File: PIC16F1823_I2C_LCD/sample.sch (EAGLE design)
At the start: 16 parts, among them CN1 12V_IN, CN2 PIC_CN_H, SW1 10-XX, U1 XC6202P502TB, U2 PIC16F1823-I/P, U3 AE-AQM1602A

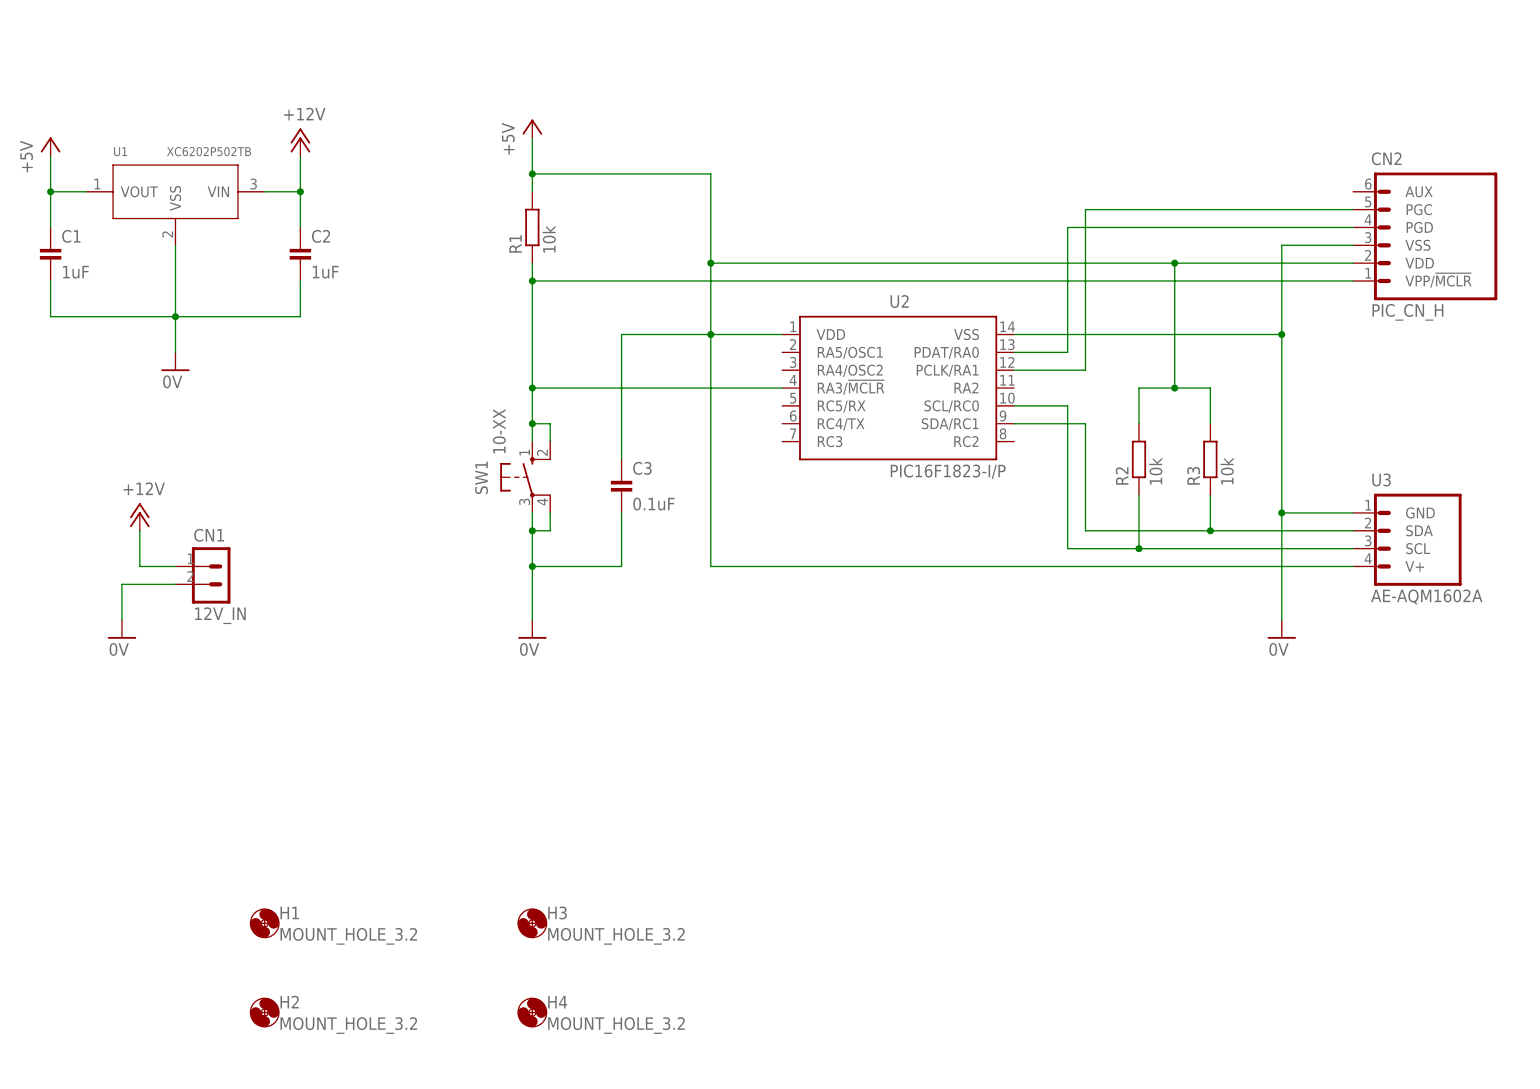
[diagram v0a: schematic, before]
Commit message: 回路図を3.3Vに修正
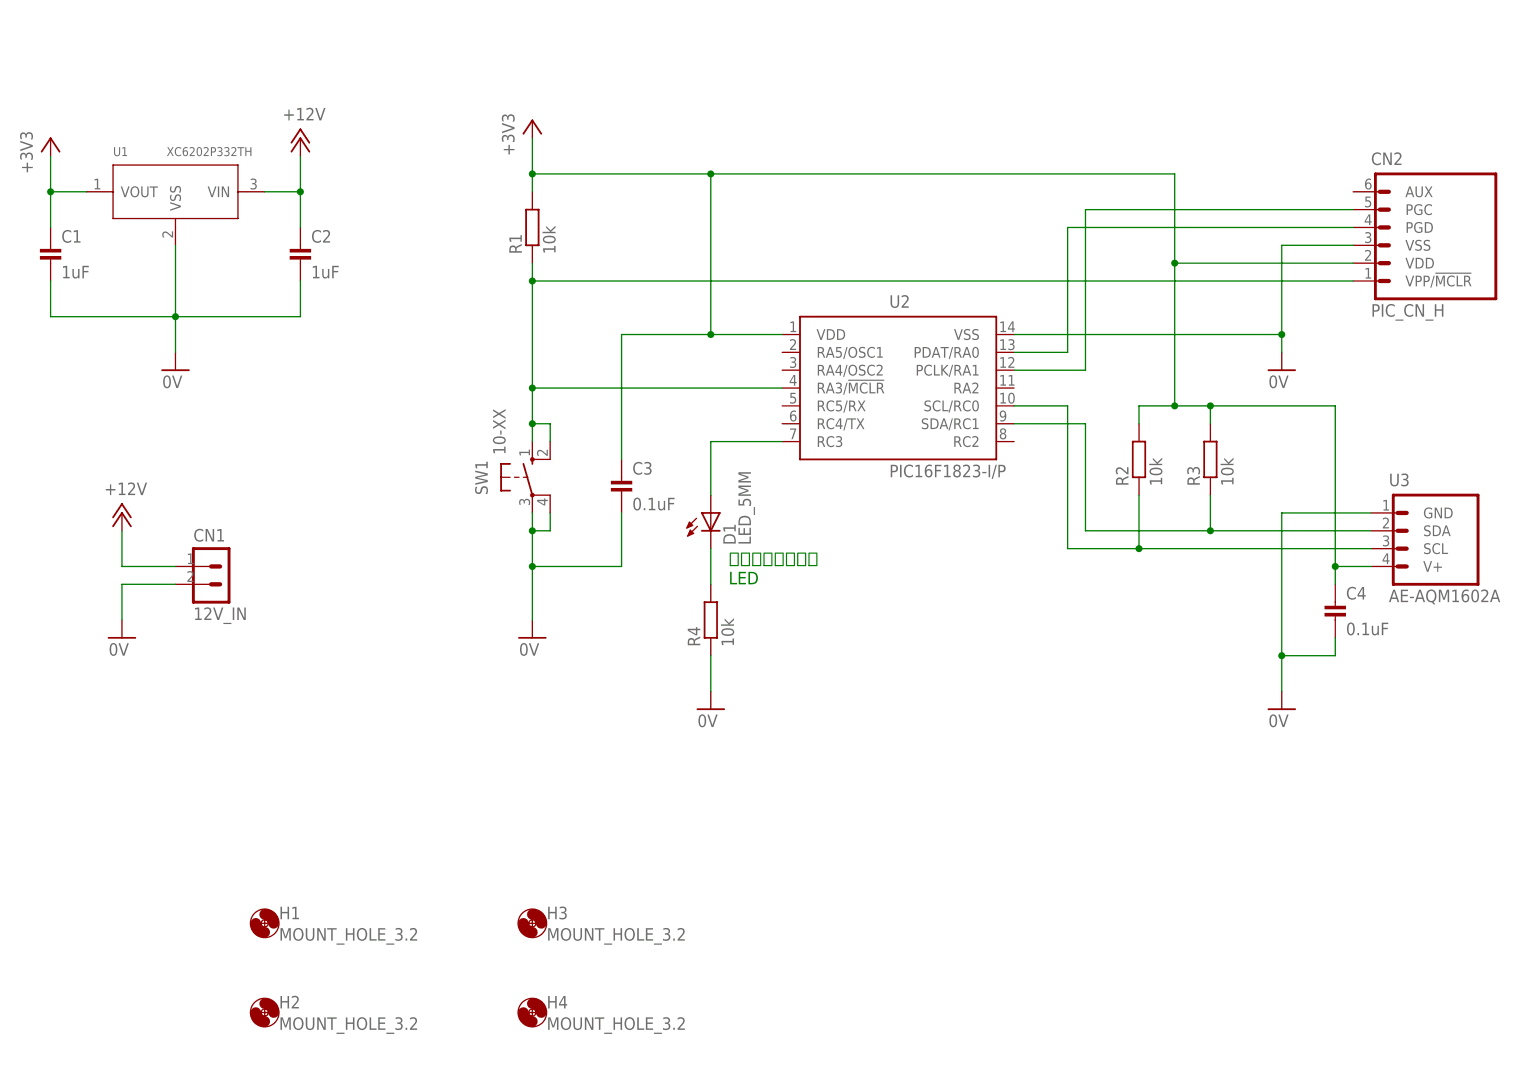
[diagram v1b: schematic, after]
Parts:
- added C4: 0.1uF, Parts:CAP_200MIL
- added D1: LED_5MM, Parts:LED_5MM
- added R4: 10k, Parts:RESISTOR_300MIL
- U1: value XC6202P502TB -> XC6202P332TH; device Parts:XC6202P502TB -> Parts:XC6202P332TH
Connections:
- removed net +5V: C1.1, C3.1, CN2.VDD, R1.2, R2.2, R3.2, U1.VOUT, U2.VDD, U3.V+
- new net +3V3: C1.1, C3.1, C4.1, CN2.VDD, R1.2, R2.2, R3.2, U1.VOUT, U2.VDD, U3.V+
- new net N$6: D1.C, R4.2
- new net N$7: D1.A, U2.RC3
- net 0V: now also C4.2, R4.1
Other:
- note added: "ヘルスチェック用 LED"
- moved on the sheet: U3

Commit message: 回路図を修正
I2Cセンサーを追加
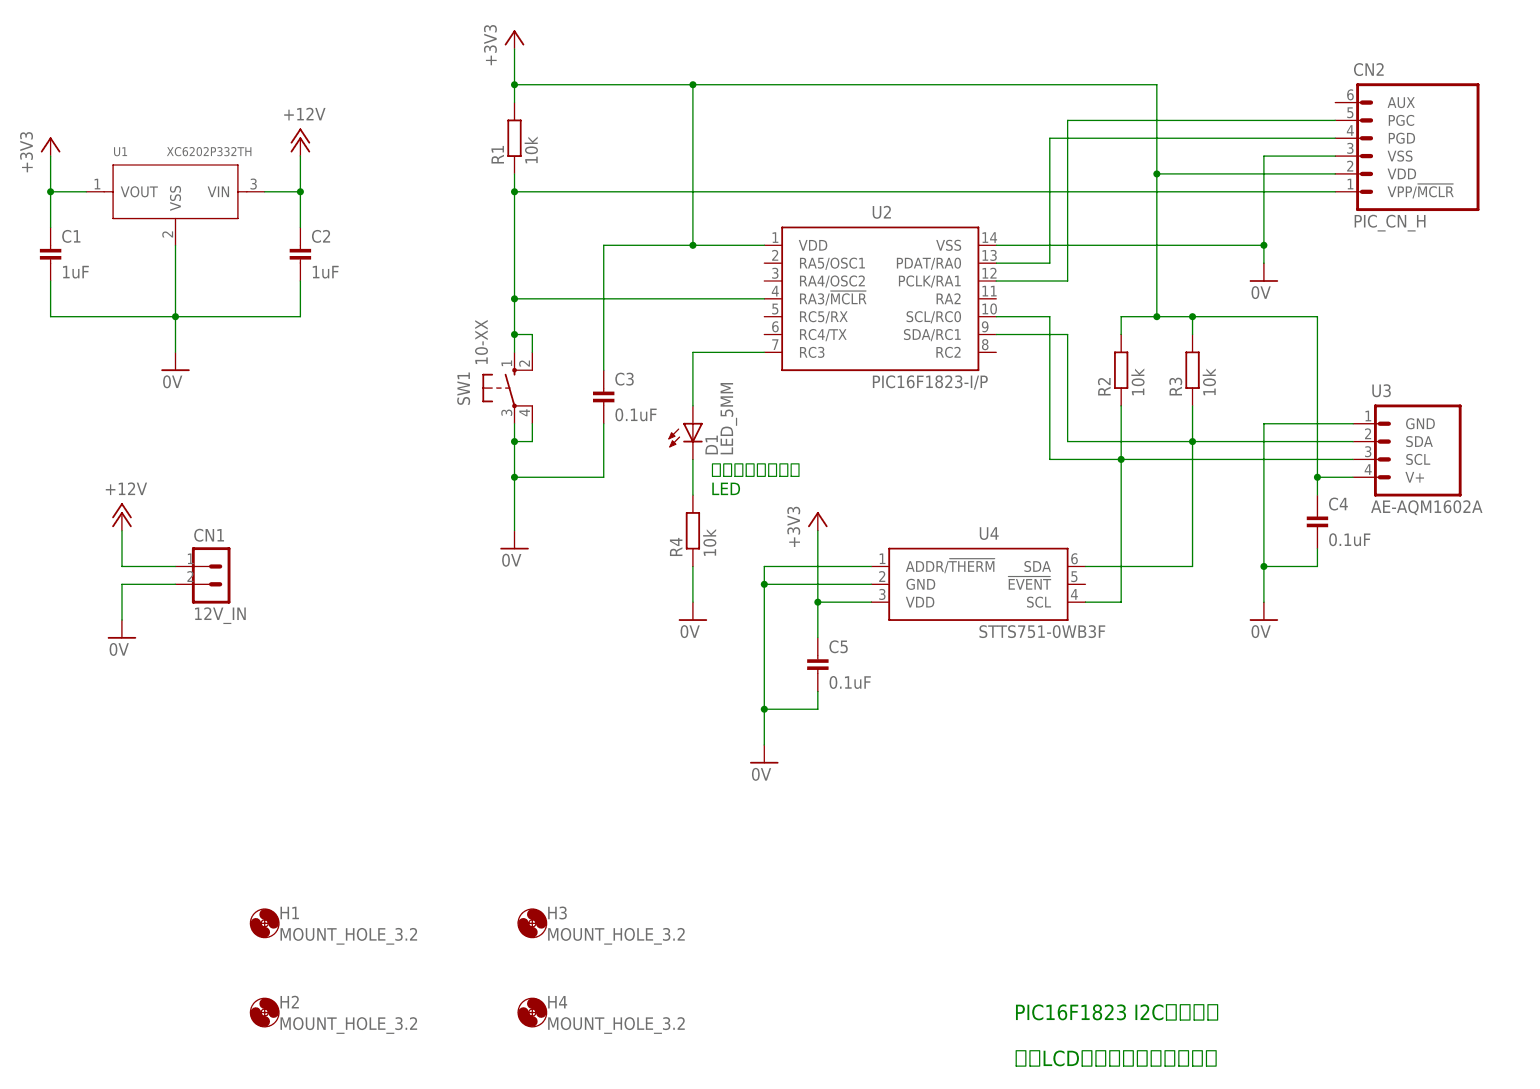
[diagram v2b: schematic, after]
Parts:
- added C5: 0.1uF, Parts:CAP_200MIL
- added U4: STTS751-0WB3F, Parts:STTS751-0WB3F
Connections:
- net +3V3: now also C5.1, U4.VDD
- net 0V: now also C5.2, U4.ADDR/!THERM!, U4.GND
- net N$1: now also U4.SDA
- net N$5: now also U4.SCL
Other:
- note added: "PIC16F1823 I2Cサンプル 小型LCDと温度センサーを接続"
- moved on the sheet: C3, C4, CN2, D1, R1, R2, R3, R4, SW1, U2, U3
